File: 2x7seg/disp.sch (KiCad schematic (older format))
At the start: 11 parts, among them P1 CONN_01X08, P2 CONN_01X08, U1 TLC59282

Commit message: Generate PDF schematics.
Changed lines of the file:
@@
 F 2 "Capacitors_SMD:C_1206_HandSoldering" H 5838 6750 30  0001 C CNN
 F 3 "" H 5800 6900 60  0000 C CNN
-F 4 "25V" H 5700 6800 60  0000 C CNN "Voltage"
+F 4 "25V" H 5700 6800 50  0000 C CNN "Voltage"
 F 5 "10%" H 5900 6700 50  0000 C CNN "Tolerance"
 F 6 "X5R" H 5700 7000 50  0000 C CNN "Dielectric"
@@
 $EndComp
 Wire Wire Line
-	1400 1800 10300 1800
-Wire Wire Line
-	1400 1900 10300 1900
-Wire Wire Line
-	1400 2000 10300 2000
-Wire Wire Line
-	1400 2200 10300 2200
-Wire Wire Line
-	1400 2300 10300 2300
-Wire Wire Line
-	1400 2400 10300 2400
-Wire Wire Line
-	1400 2500 10300 2500
-Wire Wire Line
-	4450 6400 4450 6750
+	1400 1800 3200 1800
+Wire Wire Line
+	3200 1800 4700 1800
+Wire Wire Line
+	4700 1800 10300 1800
+Wire Wire Line
+	1400 1900 1800 1900
+Wire Wire Line
+	1800 1900 5250 1900
+Wire Wire Line
+	5250 1900 10300 1900
+Wire Wire Line
+	1400 2000 1550 2000
+Wire Wire Line
+	1550 2000 10300 2000
+Wire Wire Line
+	1400 2200 2100 2200
+Wire Wire Line
+	2100 2200 10300 2200
+Wire Wire Line
+	1400 2300 2000 2300
+Wire Wire Line
+	2000 2300 10300 2300
+Wire Wire Line
+	1400 2400 2200 2400
+Wire Wire Line
+	2200 2400 9850 2400
+Wire Wire Line
+	9850 2400 10000 2400
+Wire Wire Line
+	10000 2400 10300 2400
+Wire Wire Line
+	1400 2500 1550 2500
+Wire Wire Line
+	1550 2500 1800 2500
+Wire Wire Line
+	1800 2500 5750 2500
+Wire Wire Line
+	5750 2500 10300 2500
+Wire Wire Line
+	4450 6400 4450 6600
+Wire Wire Line
+	4450 6600 4450 6750
 Wire Wire Line
 	4450 6600 4900 6600
@@
 	4900 6600 4900 6750
 Wire Wire Line
-	4450 7050 4450 7400
+	4450 7050 4450 7200
+Wire Wire Line
+	4450 7200 4450 7400
 Wire Wire Line
 	4450 7200 4900 7200
@@
 	4900 7200 4900 7050
 Wire Wire Line
-	5800 6350 5800 6750
+	5800 6350 5800 6600
+Wire Wire Line
+	5800 6600 5800 6750
 Wire Wire Line
 	5800 6600 6250 6600
@@
 	6250 7200 5800 7200
 Wire Wire Line
-	5800 7050 5800 7400
+	5800 7050 5800 7200
+Wire Wire Line
+	5800 7200 5800 7400
 $Comp
 L GND #PWR03
@@
 	3900 4300 4050 4300
 Wire Wire Line
-	4050 4300 4050 5850
-Wire Wire Line
-	4050 5850 7500 5850
-Wire Wire Line
-	7500 5850 7500 3600
+	4050 4300 4050 5900
+Wire Wire Line
+	4050 5900 7500 5900
+Wire Wire Line
+	7500 5900 7500 3600
 Wire Wire Line
 	7500 3600 8400 3600
@@
 	3900 4200 4150 4200
 Wire Wire Line
-	4150 4200 4150 5750
-Wire Wire Line
-	4150 5750 7600 5750
-Wire Wire Line
-	7600 5750 7600 3700
+	4150 4200 4150 5800
+Wire Wire Line
+	4150 5800 7600 5800
+Wire Wire Line
+	7600 5800 7600 3700
 Wire Wire Line
 	7600 3700 8400 3700
@@
 	3900 4100 4250 4100
 Wire Wire Line
-	4250 4100 4250 5650
-Wire Wire Line
-	4250 5650 7700 5650
-Wire Wire Line
-	7700 5650 7700 3800
+	4250 4100 4250 5700
+Wire Wire Line
+	4250 5700 7700 5700
+Wire Wire Line
+	7700 5700 7700 3800
 Wire Wire Line
 	7700 3800 8400 3800
@@
 	3900 4000 4350 4000
 Wire Wire Line
-	4350 4000 4350 5550
-Wire Wire Line
-	4350 5550 7800 5550
-Wire Wire Line
-	7800 5550 7800 3900
+	4350 4000 4350 5600
+Wire Wire Line
+	4350 5600 7800 5600
+Wire Wire Line
+	7800 5600 7800 3900
 Wire Wire Line
 	7800 3900 8400 3900
@@
 	8400 4000 7900 4000
 Wire Wire Line
-	7900 4000 7900 5450
-Wire Wire Line
-	7900 5450 4450 5450
-Wire Wire Line
-	4450 5450 4450 3900
+	7900 4000 7900 5500
+Wire Wire Line
+	7900 5500 4450 5500
+Wire Wire Line
+	4450 5500 4450 3900
 Wire Wire Line
 	4450 3900 3900 3900
@@
 	3900 3800 4550 3800
 Wire Wire Line
-	4550 3800 4550 5350
-Wire Wire Line
-	4550 5350 8000 5350
-Wire Wire Line
-	8000 5350 8000 4100
+	4550 3800 4550 5400
+Wire Wire Line
+	4550 5400 8000 5400
+Wire Wire Line
+	8000 5400 8000 4100
 Wire Wire Line
 	8000 4100 8400 4100
@@
 	8400 4200 8100 4200
 Wire Wire Line
-	8100 4200 8100 5250
-Wire Wire Line
-	8100 5250 4650 5250
-Wire Wire Line
-	4650 5250 4650 3700
+	8100 4200 8100 5300
+Wire Wire Line
+	8100 5300 4650 5300
+Wire Wire Line
+	4650 5300 4650 3700
 Wire Wire Line
 	4650 3700 3900 3700
@@
 	3900 3600 4750 3600
 Wire Wire Line
-	4750 3600 4750 5150
-Wire Wire Line
-	4750 5150 8200 5150
-Wire Wire Line
-	8200 5150 8200 4400
+	4750 3600 4750 5200
+Wire Wire Line
+	4750 5200 8200 5200
+Wire Wire Line
+	8200 5200 8200 4400
 Wire Wire Line
 	8200 4400 8400 4400

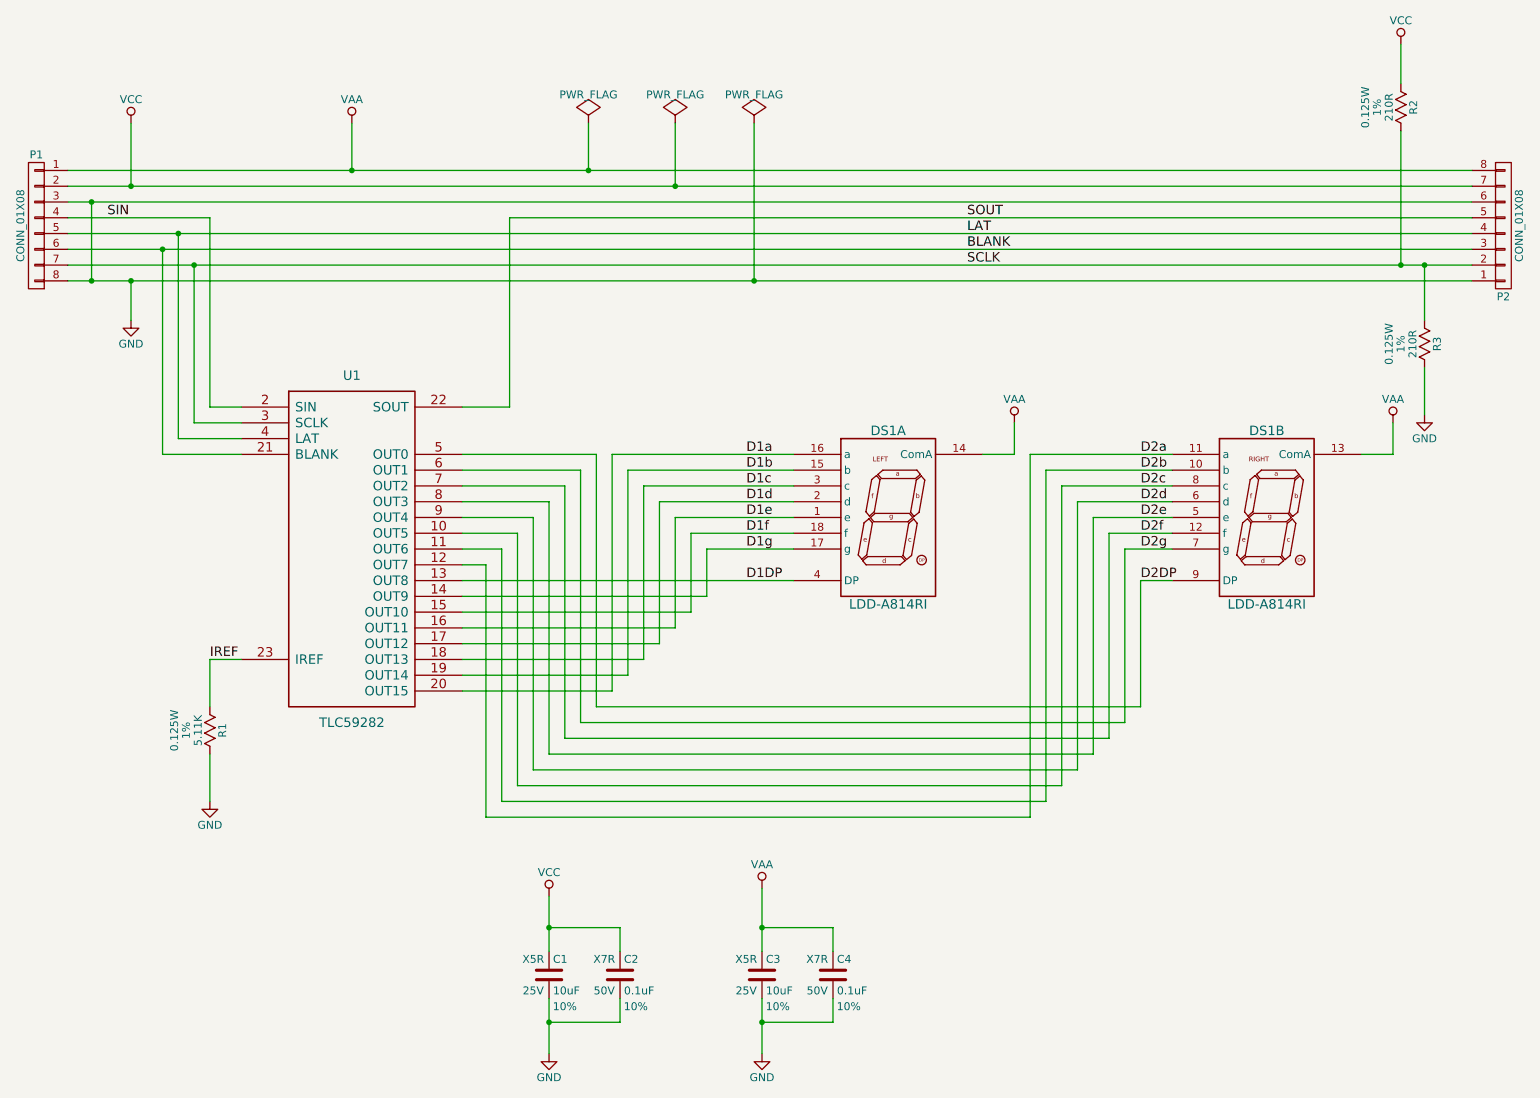
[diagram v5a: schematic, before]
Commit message: Remove termination resistors on clock line.
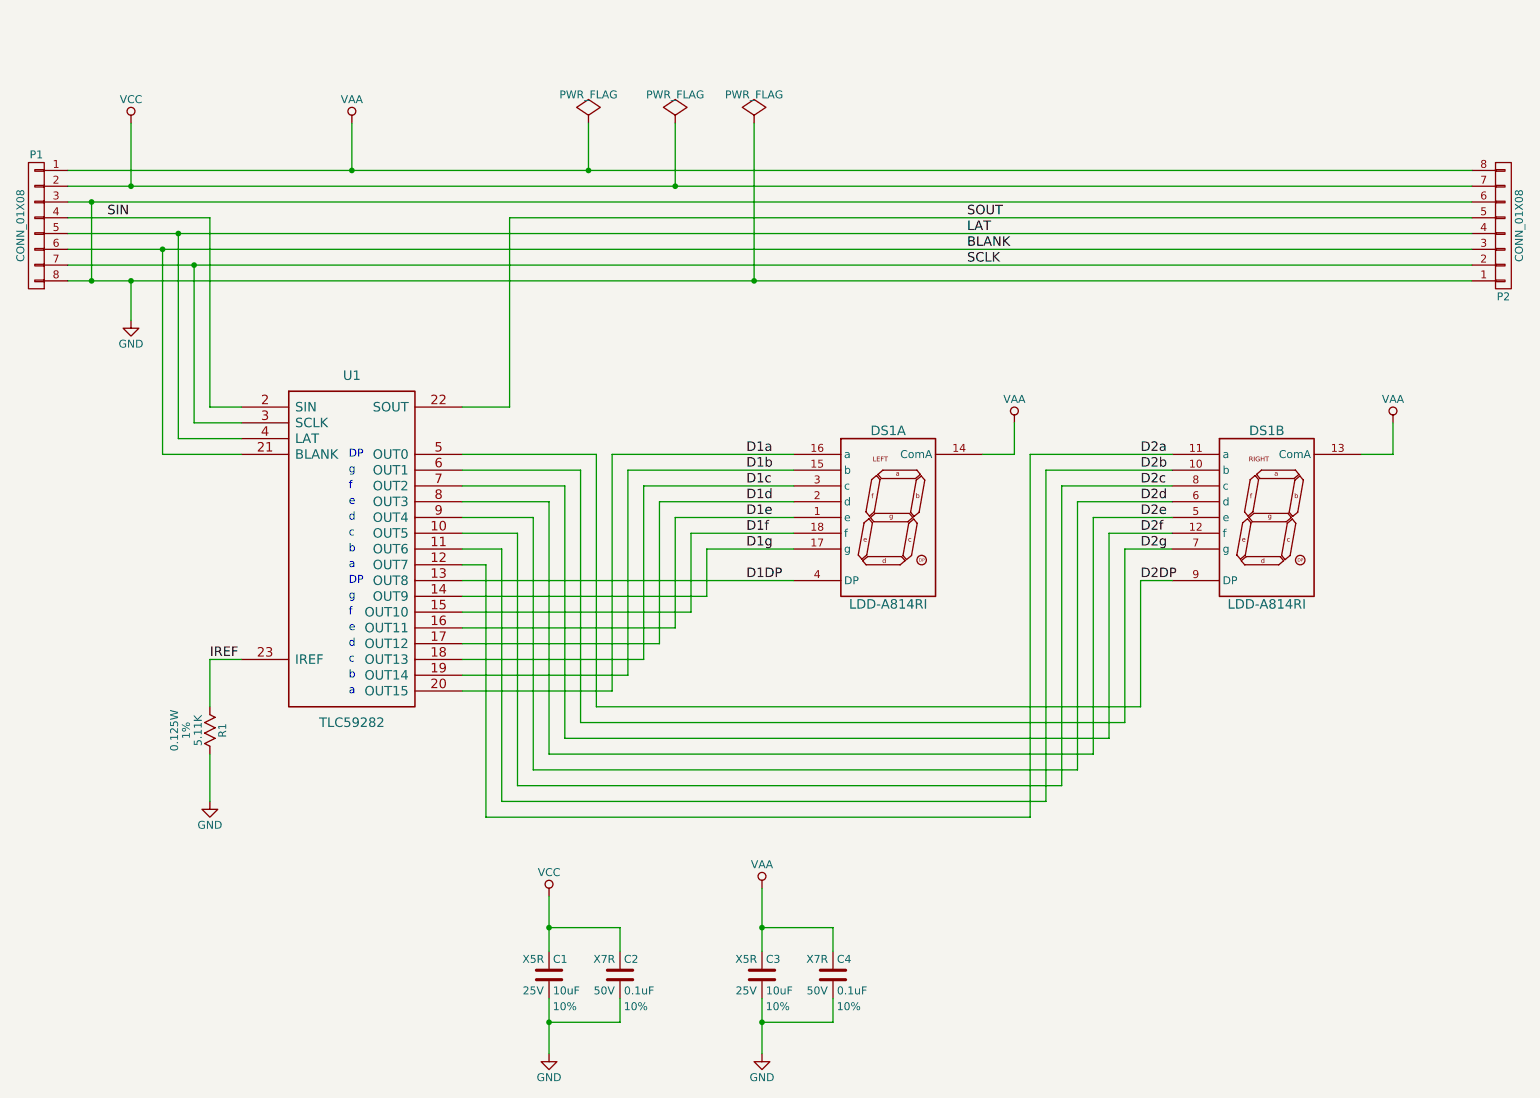
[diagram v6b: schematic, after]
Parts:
- removed R2, R3: 210R, Resistors_SMD:R_0805_HandSoldering, symbol R_local
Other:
- note added: "DP"
- note added: "a"
- note added: "b"
- note added: "c"
- note added: "d"
- note added: "e"
- note added: "f"
- note added: "g"
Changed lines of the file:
@@
 $EndComp
 Wire Wire Line
-	1400 1800 3200 1800
-Wire Wire Line
-	3200 1800 4700 1800
-Wire Wire Line
-	4700 1800 10300 1800
-Wire Wire Line
-	1400 1900 1800 1900
-Wire Wire Line
-	1800 1900 5250 1900
-Wire Wire Line
-	5250 1900 10300 1900
-Wire Wire Line
-	1400 2000 1550 2000
-Wire Wire Line
-	1550 2000 10300 2000
-Wire Wire Line
-	1400 2200 2100 2200
-Wire Wire Line
-	2100 2200 10300 2200
-Wire Wire Line
-	1400 2300 2000 2300
-Wire Wire Line
-	2000 2300 10300 2300
-Wire Wire Line
-	1400 2400 2200 2400
-Wire Wire Line
-	2200 2400 9850 2400
-Wire Wire Line
-	9850 2400 10000 2400
-Wire Wire Line
-	10000 2400 10300 2400
-Wire Wire Line
-	1400 2500 1550 2500
-Wire Wire Line
-	1550 2500 1800 2500
-Wire Wire Line
-	1800 2500 5750 2500
-Wire Wire Line
-	5750 2500 10300 2500
-Wire Wire Line
-	4450 6400 4450 6600
-Wire Wire Line
-	4450 6600 4450 6750
+	1400 1800 10300 1800
+Wire Wire Line
+	1400 1900 10300 1900
+Wire Wire Line
+	1400 2000 10300 2000
+Wire Wire Line
+	1400 2200 10300 2200
+Wire Wire Line
+	1400 2300 10300 2300
+Wire Wire Line
+	1400 2400 10300 2400
+Wire Wire Line
+	1400 2500 10300 2500
+Wire Wire Line
+	4450 6400 4450 6750
 Wire Wire Line
 	4450 6600 4900 6600
@@
 	4900 6600 4900 6750
 Wire Wire Line
-	4450 7050 4450 7200
-Wire Wire Line
-	4450 7200 4450 7400
+	4450 7050 4450 7400
 Wire Wire Line
 	4450 7200 4900 7200
@@
 	4900 7200 4900 7050
 Wire Wire Line
-	5800 6350 5800 6600
-Wire Wire Line
-	5800 6600 5800 6750
+	5800 6350 5800 6750
 Wire Wire Line
 	5800 6600 6250 6600
@@
 	6250 7200 5800 7200
 Wire Wire Line
-	5800 7050 5800 7200
-Wire Wire Line
-	5800 7200 5800 7400
+	5800 7050 5800 7400
 $Comp
 L GND #PWR03
@@
 	8200 4400 8400 4400
 $Comp
-L VCC #PWR07
-U 1 1 559820BB
-P 9850 1000
-F 0 "#PWR07" H 9850 850 50  0001 C CNN
-F 1 "VCC" H 9850 1150 50  0000 C CNN
-F 2 "" H 9850 1000 60  0000 C CNN
-F 3 "" H 9850 1000 60  0000 C CNN
-	1    9850 1000
-	1    0    0    -1
-$EndComp
-$Comp
-L GND #PWR08
-U 1 1 55982884
-P 10000 3350
-F 0 "#PWR08" H 10000 3100 50  0001 C CNN
-F 1 "GND" H 10000 3200 50  0000 C CNN
-F 2 "" H 10000 3350 60  0000 C CNN
-F 3 "" H 10000 3350 60  0000 C CNN
-	1    10000 3350
-	1    0    0    -1
-$EndComp
-Wire Wire Line
-	10000 3050 10000 3350
-Wire Wire Line
-	10000 2750 10000 2400
-Connection ~ 10000 2400
-Wire Wire Line
-	9850 1250 9850 1000
-Wire Wire Line
-	9850 1550 9850 2400
-Connection ~ 9850 2400
-$Comp
-L VAA #PWR09
+L VAA #PWR07
 U 1 1 559831F1
 P 3200 1500
-F 0 "#PWR09" H 3200 1350 50  0001 C CNN
+F 0 "#PWR07" H 3200 1350 50  0001 C CNN
 F 1 "VAA" H 3200 1650 50  0000 C CNN
 F 2 "" H 3200 1500 60  0000 C CNN
@@
 $EndComp
 $Comp
-L VAA #PWR010
+L VAA #PWR08
 U 1 1 559832E2
 P 9800 3400
-F 0 "#PWR010" H 9800 3250 50  0001 C CNN
+F 0 "#PWR08" H 9800 3250 50  0001 C CNN
 F 1 "VAA" H 9800 3550 50  0000 C CNN
 F 2 "" H 9800 3400 60  0000 C CNN
@@
 	9800 3600 9600 3600
 $Comp
-L VAA #PWR011
+L VAA #PWR09
 U 1 1 559842A3
 P 5800 6350
-F 0 "#PWR011" H 5800 6200 50  0001 C CNN
+F 0 "#PWR09" H 5800 6200 50  0001 C CNN
 F 1 "VAA" H 5800 6500 50  0000 C CNN
 F 2 "" H 5800 6350 60  0000 C CNN
@@
 Connection ~ 5800 6600
 $Comp
-L VAA #PWR012
+L VAA #PWR010
 U 1 1 559843C1
 P 7400 3400
-F 0 "#PWR012" H 7400 3250 50  0001 C CNN
+F 0 "#PWR010" H 7400 3250 50  0001 C CNN
 F 1 "VAA" H 7400 3550 50  0000 C CNN
 F 2 "" H 7400 3400 60  0000 C CNN
@@
 	7400 3600 7200 3600
 $Comp
-L PWR_FLAG #FLG013
+L PWR_FLAG #FLG011
 U 1 1 559854F7
 P 4700 1500
-F 0 "#FLG013" H 4700 1595 50  0001 C CNN
+F 0 "#FLG011" H 4700 1595 50  0001 C CNN
 F 1 "PWR_FLAG" H 4700 1680 50  0000 C CNN
 F 2 "" H 4700 1500 60  0000 C CNN
@@
 	4700 1500 4700 1800
 $Comp
-L PWR_FLAG #FLG014
+L PWR_FLAG #FLG012
 U 1 1 55985759
 P 5250 1500
-F 0 "#FLG014" H 5250 1595 50  0001 C CNN
+F 0 "#FLG012" H 5250 1595 50  0001 C CNN
 F 1 "PWR_FLAG" H 5250 1680 50  0000 C CNN
 F 2 "" H 5250 1500 60  0000 C CNN
@@
 $EndComp
 $Comp
-L PWR_FLAG #FLG015
+L PWR_FLAG #FLG013
 U 1 1 5598594E
 P 5750 1500
-F 0 "#FLG015" H 5750 1595 50  0001 C CNN
+F 0 "#FLG013" H 5750 1595 50  0001 C CNN
 F 1 "PWR_FLAG" H 5750 1680 50  0000 C CNN
 F 2 "" H 5750 1500 60  0000 C CNN
@@
 $EndComp
 $Comp
-L R_local R2
-U 1 1 562F083B
-P 9850 1400
-F 0 "R2" V 9930 1400 50  0000 C CNN
-F 1 "210R" V 9775 1400 50  0000 C CNN
-F 2 "Resistors_SMD:R_0805_HandSoldering" V 9780 1400 30  0001 C CNN
-F 3 "" V 9930 1400 30  0000 C CNN
-F 4 "1%" V 9700 1400 50  0000 C CNN "Tolerance"
-F 5 "0.125W" V 9625 1400 50  0000 C CNN "Power"
-F 6 "Vishay Dale" V 9850 1400 50  0001 C CNN "Manufacturer"
-F 7 "CRCW0805210RFKEA" V 10000 1400 50  0001 C CNN "PartNum"
-	1    9850 1400
-	1    0    0    -1
-$EndComp
-$Comp
-L R_local R3
-U 1 1 562F0AB4
-P 10000 2900
-F 0 "R3" V 10080 2900 50  0000 C CNN
-F 1 "210R" V 9925 2900 50  0000 C CNN
-F 2 "Resistors_SMD:R_0805_HandSoldering" V 9930 2900 30  0001 C CNN
-F 3 "" V 10080 2900 30  0000 C CNN
-F 4 "1%" V 9850 2900 50  0000 C CNN "Tolerance"
-F 5 "0.125W" V 9775 2900 50  0000 C CNN "Power"
-F 6 "Vishay Dale" V 10000 2900 50  0001 C CNN "Manufacturer"
-F 7 "CRCW0805210RFKEA" V 10150 2900 50  0001 C CNN "PartNum"
-	1    10000 2900
-	1    0    0    -1
-$EndComp
-$Comp
 L LDD-A814RI DS1
 U 2 1 562F101C
@@
 	1    0    0    -1
 $EndComp
+Text Notes 3180 5130 0    50   ~ 0
+a
+Text Notes 3180 5030 0    50   ~ 0
+b
+Text Notes 3180 4930 0    50   ~ 0
+c
+Text Notes 3180 4830 0    50   ~ 0
+d
+Text Notes 3180 4730 0    50   ~ 0
+e
+Text Notes 3180 4630 0    50   ~ 0
+f
+Text Notes 3180 4530 0    50   ~ 0
+g
+Text Notes 3180 4430 0    50   ~ 0
+DP
+Text Notes 3180 4330 0    50   ~ 0
+a
+Text Notes 3180 4230 0    50   ~ 0
+b
+Text Notes 3180 4130 0    50   ~ 0
+c
+Text Notes 3180 4030 0    50   ~ 0
+d
+Text Notes 3180 3930 0    50   ~ 0
+e
+Text Notes 3180 3830 0    50   ~ 0
+f
+Text Notes 3180 3730 0    50   ~ 0
+g
+Text Notes 3180 3630 0    50   ~ 0
+DP
 $EndSCHEMATC

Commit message: Change footprints for 0805 and 1206 packages.
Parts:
- C1, C3: footprint Capacitors_SMD:C_1206_HandSoldering -> local:C_1206_HandSoldering
- C2, C4: footprint Capacitors_SMD:C_0805_HandSoldering -> local:C_0805_HandSoldering
- R1: footprint Resistors_SMD:R_0805_HandSoldering -> local:R_0805_HandSoldering
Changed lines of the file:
@@
 F 0 "C1" H 4475 7000 50  0000 L CNN
 F 1 "10uF" H 4475 6800 50  0000 L CNN
-F 2 "Capacitors_SMD:C_1206_HandSoldering" H 4488 6750 30  0001 C CNN
+F 2 "local:C_1206_HandSoldering" H 4488 6750 30  0001 C CNN
 F 3 "" H 4450 6900 60  0000 C CNN
 F 4 "25V" H 4350 6800 50  0000 C CNN "Voltage"
@@
 F 0 "C2" H 4925 7000 50  0000 L CNN
 F 1 "0.1uF" H 4925 6800 50  0000 L CNN
-F 2 "Capacitors_SMD:C_0805_HandSoldering" H 4938 6750 30  0001 C CNN
+F 2 "local:C_0805_HandSoldering" H 4938 6750 30  0001 C CNN
 F 3 "" H 4900 6900 60  0000 C CNN
 F 4 "50V" H 4800 6800 50  0000 C CNN "Voltage"
@@
 F 0 "C3" H 5825 7000 50  0000 L CNN
 F 1 "10uF" H 5825 6800 50  0000 L CNN
-F 2 "Capacitors_SMD:C_1206_HandSoldering" H 5838 6750 30  0001 C CNN
+F 2 "local:C_1206_HandSoldering" H 5838 6750 30  0001 C CNN
 F 3 "" H 5800 6900 60  0000 C CNN
 F 4 "25V" H 5700 6800 50  0000 C CNN "Voltage"
@@
 F 0 "R1" V 2380 5350 50  0000 C CNN
 F 1 "5.11K" V 2225 5350 50  0000 C CNN
-F 2 "Resistors_SMD:R_0805_HandSoldering" V 2230 5350 30  0001 C CNN
+F 2 "local:R_0805_HandSoldering" V 2230 5350 30  0001 C CNN
 F 3 "" V 2380 5350 30  0000 C CNN
 F 4 "1%" V 2150 5350 50  0000 C CNN "Tolerance"
@@
 F 0 "C4" H 6275 7000 50  0000 L CNN
 F 1 "0.1uF" H 6275 6800 50  0000 L CNN
-F 2 "Capacitors_SMD:C_0805_HandSoldering" H 6288 6750 30  0001 C CNN
+F 2 "local:C_0805_HandSoldering" H 6288 6750 30  0001 C CNN
 F 3 "" H 6250 6900 60  0000 C CNN
 F 4 "50V" H 6150 6800 50  0000 C CNN "Voltage"
